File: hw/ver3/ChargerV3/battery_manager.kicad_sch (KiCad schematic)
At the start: 1 part, among them J7 BalanceConnector

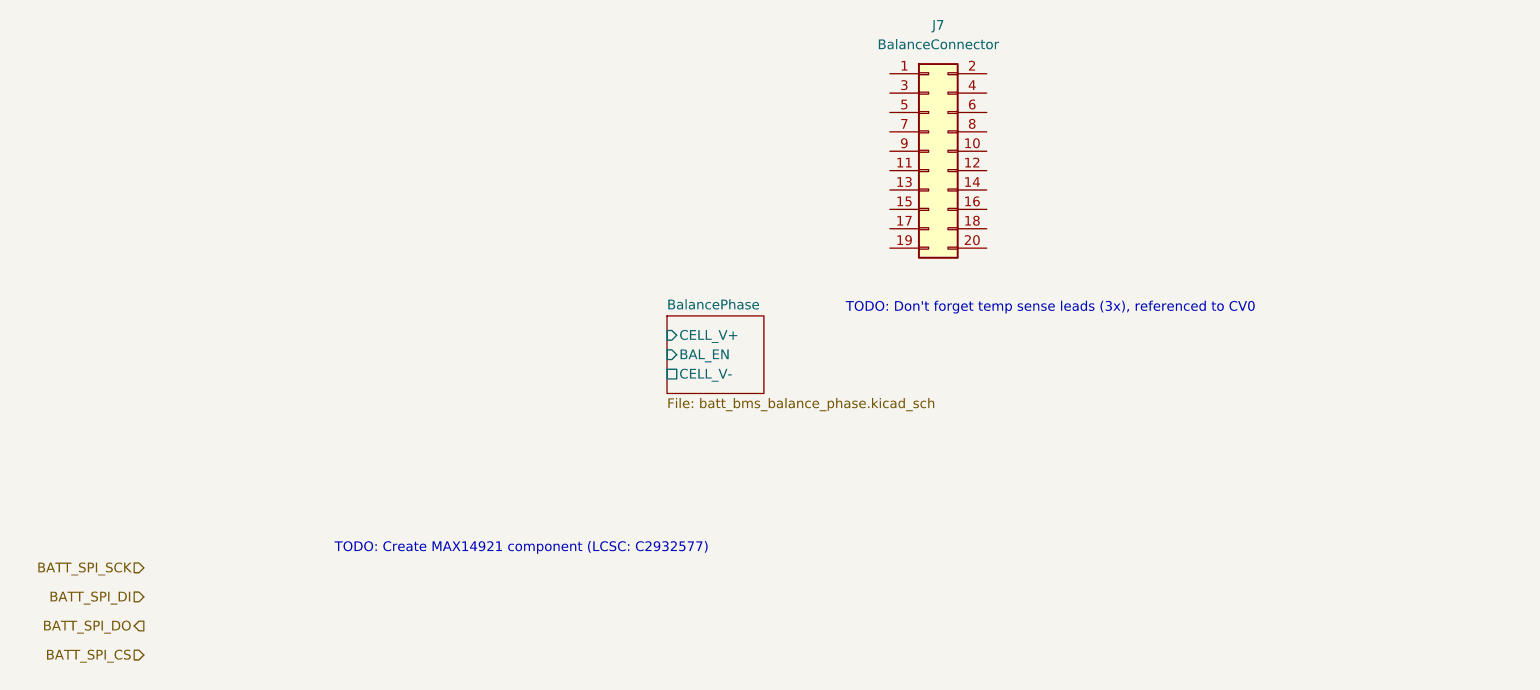
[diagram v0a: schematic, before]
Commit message: Split the design into four major components. Start working on system architecture.
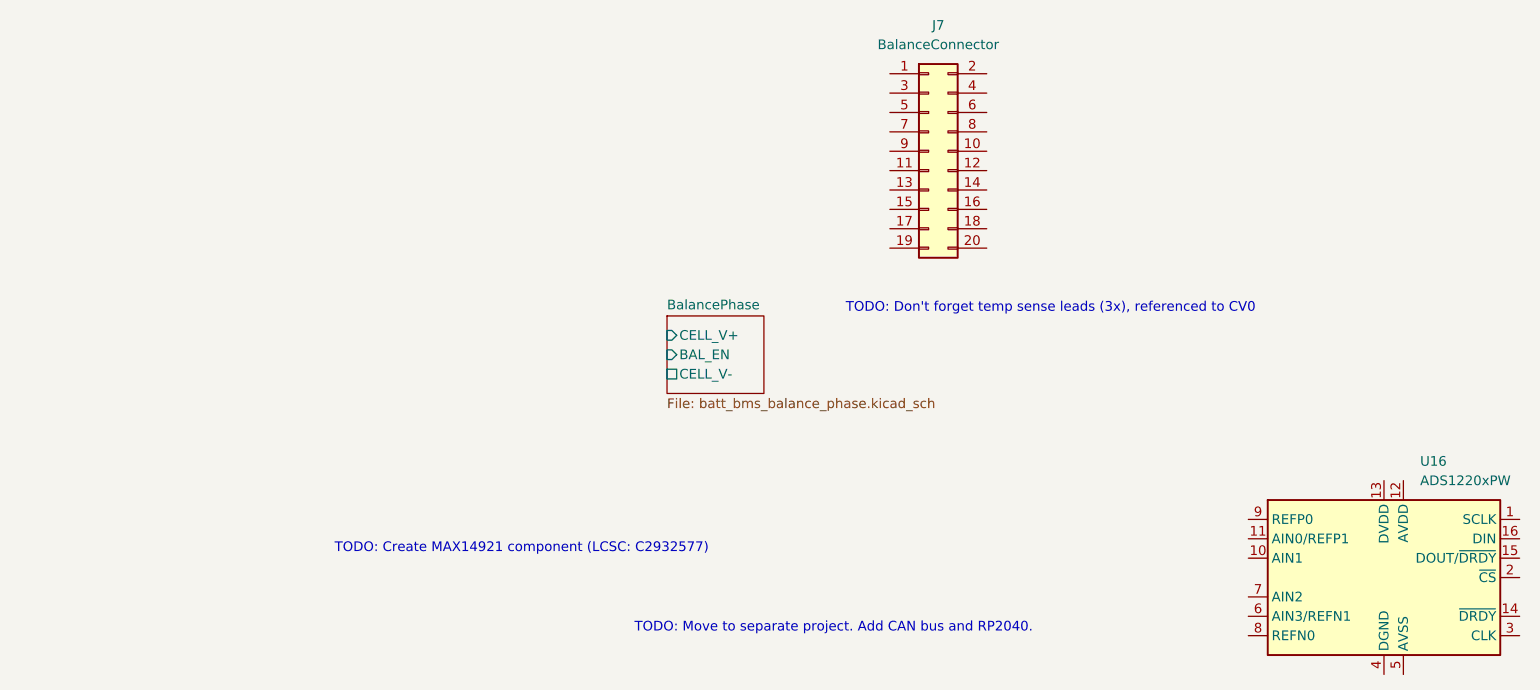
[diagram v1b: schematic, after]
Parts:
- added U16: ADS1220xPW, Package_SO:TSSOP-16_4.4x5mm_P0.65mm, symbol Analog_ADC:ADS1220xPW
- J7: footprint (none) -> Connector_IDC:IDC-Header_2x10_P2.54mm_Vertical
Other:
- note added: "TODO: Move to separate project. Add CAN bus and RP2040."
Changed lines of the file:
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@@
 	(generator_version "9.0")
 	(paper "A4")
+	(text "TODO: Move to separate project. Add CAN bus and RP2040."
+		(exclude_from_sim no)
+		(at 186.944 104.394 0)
+		(effects
+			(font
+				(size 1.27 1.27)
+			)
+		)
+	)
 	(text "TODO: Create MAX14921 component (LCSC: C2932577)"
 		(exclude_from_sim no)
@@
 		)
 	)
-	(hierarchical_label "BATT_SPI_SCK"
-		(shape input)
-		(at 96.52 96.52 180)
-		(effects
-			(font
-				(size 1.27 1.27)
+	(symbol
+		(lib_id "Analog_ADC:ADS1220xPW")
+		(at 259.08 97.79 0)
+		(unit 1)
+		(exclude_from_sim no)
+		(in_bom yes)
+		(on_board yes)
+		(dnp no)
+		(fields_autoplaced yes)
+		(property "Reference" "U16"
+			(at 263.8141 82.55 0)
+			(effects
+				(font
+					(size 1.27 1.27)
+				)
+				(justify left)
 			)
-			(justify right)
 		)
-	)
-	(hierarchical_label "BATT_SPI_CS"
-		(shape input)
-		(at 96.52 107.95 180)
-		(effects
-			(font
-				(size 1.27 1.27)
+		(property "Value" "ADS1220xPW"
+			(at 263.8141 85.09 0)
+			(effects
+				(font
+					(size 1.27 1.27)
+				)
+				(justify left)
 			)
-			(justify right)
 		)
-	)
-	(hierarchical_label "BATT_SPI_DO"
-		(shape output)
-		(at 96.52 104.14 180)
-		(effects
-			(font
-				(size 1.27 1.27)
+		(property "Footprint" "Package_SO:TSSOP-16_4.4x5mm_P0.65mm"
+			(at 265.43 83.82 0)
+			(effects
+				(font
+					(size 1.27 1.27)
+				)
+				(justify left)
+				(hide yes)
 			)
-			(justify right)
 		)
-	)
-	(hierarchical_label "BATT_SPI_DI"
-		(shape input)
-		(at 96.52 100.33 180)
-		(effects
-			(font
-				(size 1.27 1.27)
+		(property "Datasheet" "http://www.ti.com/lit/ds/symlink/ads1220.pdf"
+			(at 246.38 87.63 0)
+			(effects
+				(font
+					(size 1.27 1.27)
+				)
+				(hide yes)
 			)
-			(justify right)
+		)
+		(property "Description" "Low-power, quad-input, 24-bit analog to digital converter, integrated temperature sensor, SPI interface, TSSOP-16 package"
+			(at 259.08 97.79 0)
+			(effects
+				(font
+					(size 1.27 1.27)
+				)
+				(hide yes)
+			)
+		)
+		(property "LCSC" "C48263"
+			(at 259.08 97.79 0)
+			(effects
+				(font
+					(size 1.27 1.27)
+				)
+				(hide yes)
+			)
+		)
+		(property "JLCPCB Rotation Offset" ""
+			(at 259.08 97.79 0)
+			(effects
+				(font
+					(size 1.27 1.27)
+				)
+				(hide yes)
+			)
+		)
+		(property "DigiKey" ""
+			(at 259.08 97.79 0)
+			(effects
+				(font
+					(size 1.27 1.27)
+				)
+				(hide yes)
+			)
+		)
+		(pin "11"
+		)
+		(pin "1"
+		)
+		(pin "16"
+		)
+		(pin "12"
+		)
+		(pin "10"
+		)
+		(pin "9"
+		)
+		(pin "2"
+		)
+		(pin "7"
+		)
+		(pin "3"
+		)
+		(pin "8"
+		)
+		(pin "4"
+		)
+		(pin "6"
+		)
+		(pin "5"
+		)
+		(pin "14"
+		)
+		(pin "15"
+		)
+		(pin "13"
+		)
+		(instances
+			(project "IchnaeaV3"
+				(path "/93408532-1ffa-463d-873c-16289d2b7987/f8cdf9d7-add1-4ff8-8430-918a71e3d1f9/15949d39-4147-469d-a992-c4b48798ba19"
+					(reference "U16")
+					(unit 1)
+				)
+			)
 		)
 	)
@@
 			)
 		)
-		(property "Footprint" ""
+		(property "Footprint" "Connector_IDC:IDC-Header_2x10_P2.54mm_Vertical"
 			(at 199.39 41.91 0)
 			(effects
